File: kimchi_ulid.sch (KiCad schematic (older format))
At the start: 21 parts, among them J1 DF40HC(3.5)-60DS, J2 DF40HC(3.5)-60DS, J3 KUSBX-AS1N-B, J4 54-00176, J5 SGTL5000XNLA3, SW1 TL3301NF260QG, SW2 TL3301NF260QG, SW3 TL3301NF260QG, SW4 TL3301NF260QG, SW5 TL3301NF260QG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

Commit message: added resistors for codec, transferring workstations
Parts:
- added C? (x2): T491A105K010AT, kimchi_ulid:C1206, symbol kimchi_ulid:T491A105K010AT
- added C? (x3): C0402C104K9PACTU, kimchi_ulid:C0402, symbol kimchi_ulid:C0402C104K9PACTU
- J1, J2: symbol Connector_Generic:Conn_02x30_Counter_Clockwise -> kimchi_ulid-rescue:Conn_02x30_Counter_Clockwise-Connector_Generic
- U1: symbol Memory_EEPROM:24LC16 -> kimchi_ulid-rescue:24LC16-Memory_EEPROM
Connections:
- wire segments 69 -> 83
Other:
- moved on the sheet: J5, SW1, SW2, SW3, SW4, SW5, SW6, SW7, SW8

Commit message: Oscillator Circuit
Oscillator circuit and related components added to the codec circuit. These may be unnecessary but are pending review.
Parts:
- removed J3: KUSBX-AS1N-B, kimchi_ulid:USB_A, symbol kimchi_ulid:KUSBX-AS1N-B
- removed J4: 54-00176, kimchi_ulid:54-00176, symbol kimchi_ulid:54-00176
- added C1, C2, C?: C0402C104K9PACTU, kimchi_ulid:C0402, symbol kimchi_ulid:C0402C104K9PACTU
- added C8, C9: T491A105K010AT, kimchi_ulid:C1206, symbol kimchi_ulid:T491A105K010AT
- added J3: 1-292303-6, kimchi_ulid:TE_1-292303-6, symbol kimchi_ulid:1-292303-6
- added J4: 54-00177, kimchi_ulid:54-00177, symbol kimchi_ulid:54-00177
- added R1: RC0402JR-072K2L, AVR-KiCAD-Lib-Resistors:R0402, symbol kimchi_ulid:RC0402JR-072K2L
- added U?: SN74LV1T34DBVRG4, kimchi_ulid:SOT-23-5, symbol kimchi_ulid:SN74LV1T34DBVRG4
- added X1: ASFL1-12.288MHZ-EC-T, kimchi_ulid:ASFL1, symbol kimchi_ulid:ASFL1-12.288MHZ-EC-T
- gave numbers to parts that had none: 5
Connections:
- net labels added: SPEAKER_L, SPEAKER_R
- wire segments 83 -> 106
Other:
- moved on the sheet: C3, C4, C5, C6, C7, J5, JS1, JS2, SW1, SW2, SW3, SW4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

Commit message: Design Refactor and Major Progress
Refactored the design of the lid, integrated the schematics from the Display lid, and the HiFi lid. Changed PCB shape to reflect change to dual screen design. Found SPI TFT display for bottom display. Library updated with component footprints for new parts, and library errors and issues from importing parts from other projects resolved.
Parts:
- removed C1, C2, C3, C4, C5, C?: C0402C104K9PACTU, kimchi_ulid:C0402, symbol kimchi_ulid:C0402C104K9PACTU
- removed C6, C7, C8, C9: T491A105K010AT, kimchi_ulid:C1206, symbol kimchi_ulid:T491A105K010AT
- removed J3: 1-292303-6, kimchi_ulid:TE_1-292303-6, symbol kimchi_ulid:1-292303-6
- removed J4: 54-00177, kimchi_ulid:54-00177, symbol kimchi_ulid:54-00177
- removed J5: SGTL5000XNLA3, kimchi_ulid:QFN40P300X300X60-21N, symbol kimchi_ulid:SGTL5000XNLA3
- removed JS1, JS2: Keyes_HW-504, kimchi_ulid:Keyes_JoyStick, symbol kimchi_ulid:Keyes_HW-504
- removed R1: RC0402JR-072K2L, AVR-KiCAD-Lib-Resistors:R0402, symbol kimchi_ulid:RC0402JR-072K2L
- removed SW1, SW2, SW3, SW4, SW5, SW6, SW7, SW8: TL3301NF260QG, kimchi_ulid:TL3301NF260QG, symbol kimchi_ulid:TL3301NF260QG
- removed U?: SN74LV1T34DBVRG4, kimchi_ulid:SOT-23-5, symbol kimchi_ulid:SN74LV1T34DBVRG4
- removed X1: ASFL1-12.288MHZ-EC-T, kimchi_ulid:ASFL1, symbol kimchi_ulid:ASFL1-12.288MHZ-EC-T
- renumbered H3 to H2, H2 to H3, J1 to J2, J2 to J3

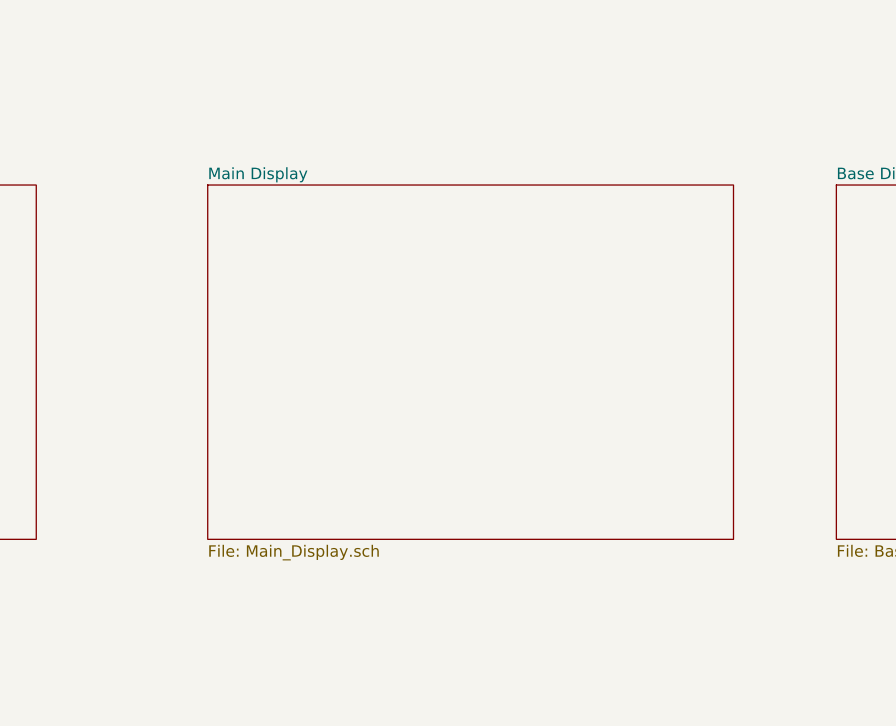
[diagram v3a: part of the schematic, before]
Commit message: Two Projects
Created a dedicated project for the upper screen PCB, I moved the IMU and USB A host circuits to their own schematic page and made them part of the PCB project for the bottom half PCB that holds the SPI touch screen, controls, battery, and Kimchi module.
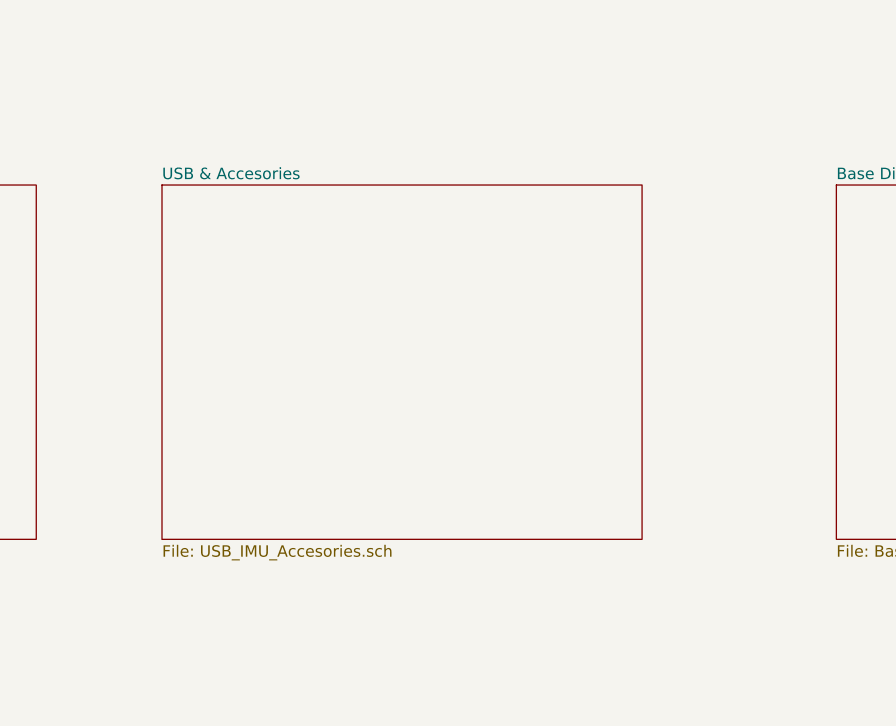
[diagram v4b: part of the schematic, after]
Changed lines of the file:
@@
-$EndSheet
-$Sheet
-S 6350 5700 2300 1550
-U 602973BC
-F0 "Main Display " 50
-F1 "Main_Display.sch" 50
 $EndSheet
 $Sheet
@@
 F1 "Base_Display_Controls.sch" 50
 $EndSheet
+$Sheet
+S 6150 5700 2100 1550
+U 603637CD
+F0 "USB & Accesories" 50
+F1 "USB_IMU_Accesories.sch" 50
+$EndSheet
 $EndSCHEMATC
